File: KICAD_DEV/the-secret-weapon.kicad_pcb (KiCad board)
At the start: 6 copper layers, 150 x 150 mm, 43 parts, among them J1 USB_C_Receptacle_USB2.0_14P, J2 Screw_Terminal_01x02, SW1 SW_Push, SW2 SW_Push, U1 STM32H743VITx, U2 USBLC6-2SC6, U3 LMR33640ADDA, U4 LM1086S-3.3/TR, Y1 8 MHz, Y2 32.768 KHz

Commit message: heading to school!
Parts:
- moved F1 3.96 mm to (168.8, 165.2)
- moved J2 3.03 mm to (166.6, 172.9)
- moved C3 2.47 mm to (150.4, 170.1), turned to 90 degrees
- moved C1 2.20 mm to (156.6, 173.0), turned to 0 degrees
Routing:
- net Net-(U3-FB): track 0.00 -> 1.62 mm
- net GND: track 4.62 -> 3.56 mm, vias 8 -> 6

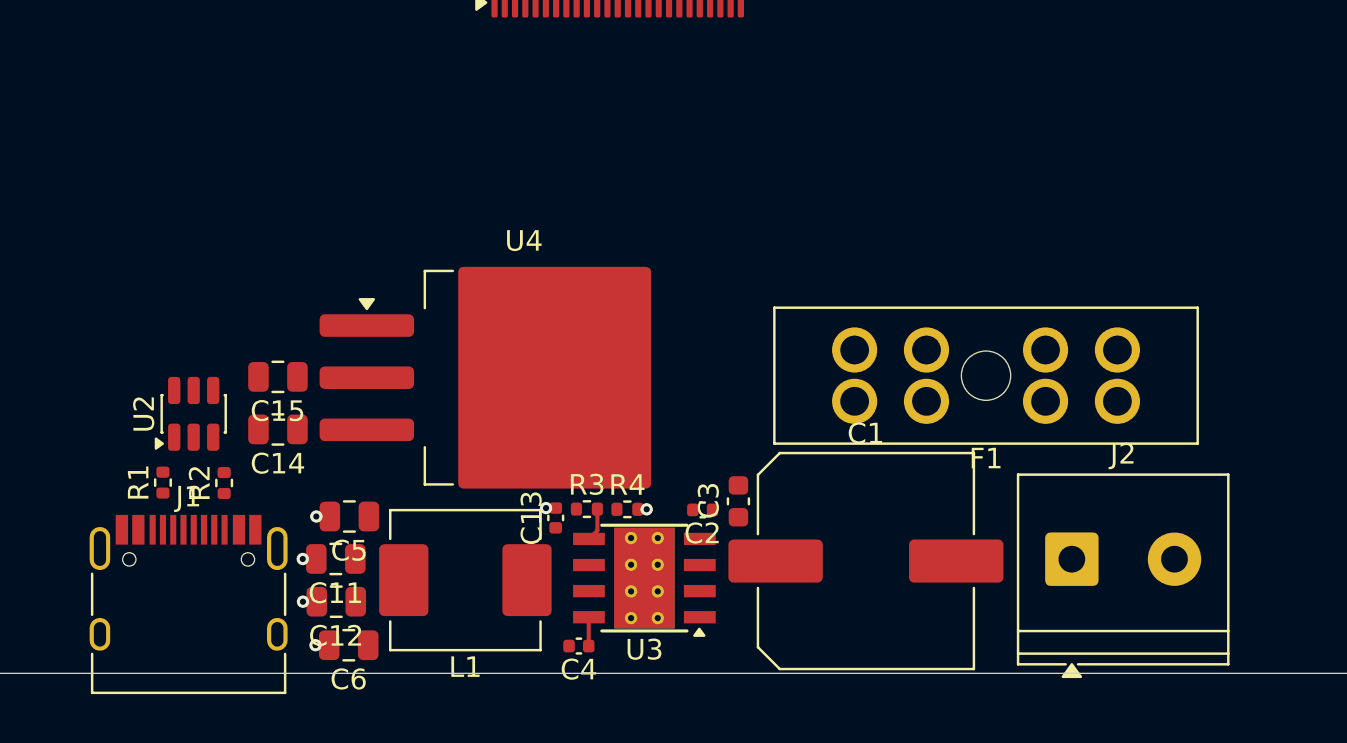
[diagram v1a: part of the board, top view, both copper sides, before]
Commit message: grounding and working on power, added the 100uF cap
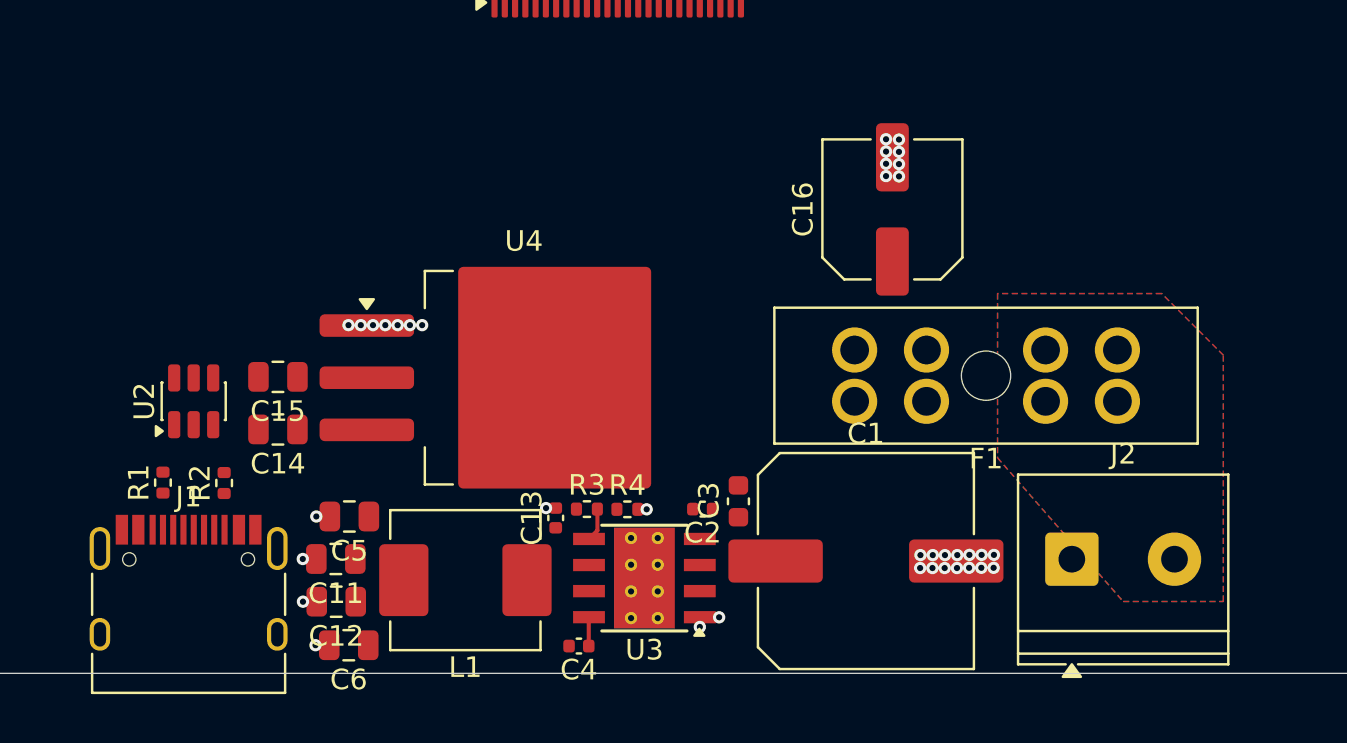
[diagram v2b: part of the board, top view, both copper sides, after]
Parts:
- added C16: 100uF, Capacitor_SMD:C_Elec_6.3x5.8, F.Cu at (157.9, 155.9)
- moved U2 0.61 mm to (123.8, 165.2)
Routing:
- net GND: track 3.56 -> 4.98 mm, vias 6 -> 37
- added copper zone on B.Cu, net Net-(J2-Pin_2)
- added copper zone on F.Cu, net Net-(J2-Pin_2)

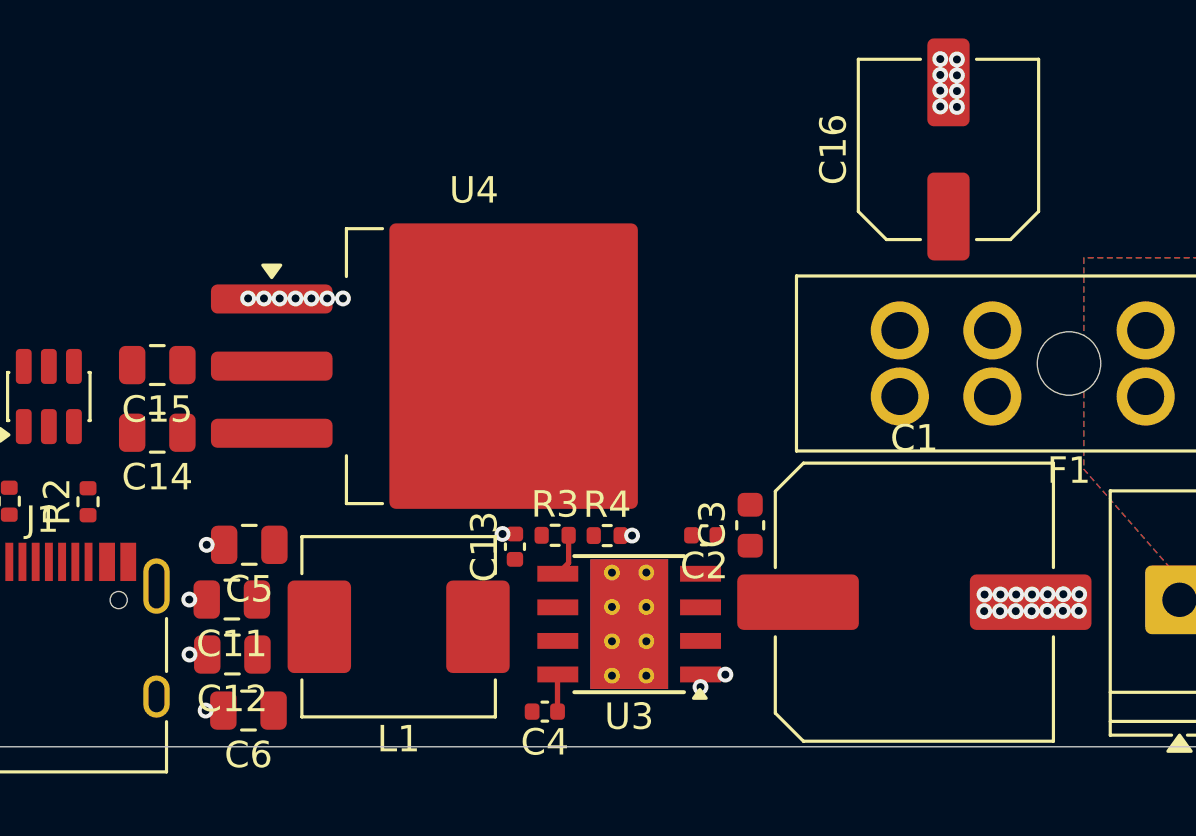
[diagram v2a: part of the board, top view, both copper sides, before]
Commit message: adding the power fills
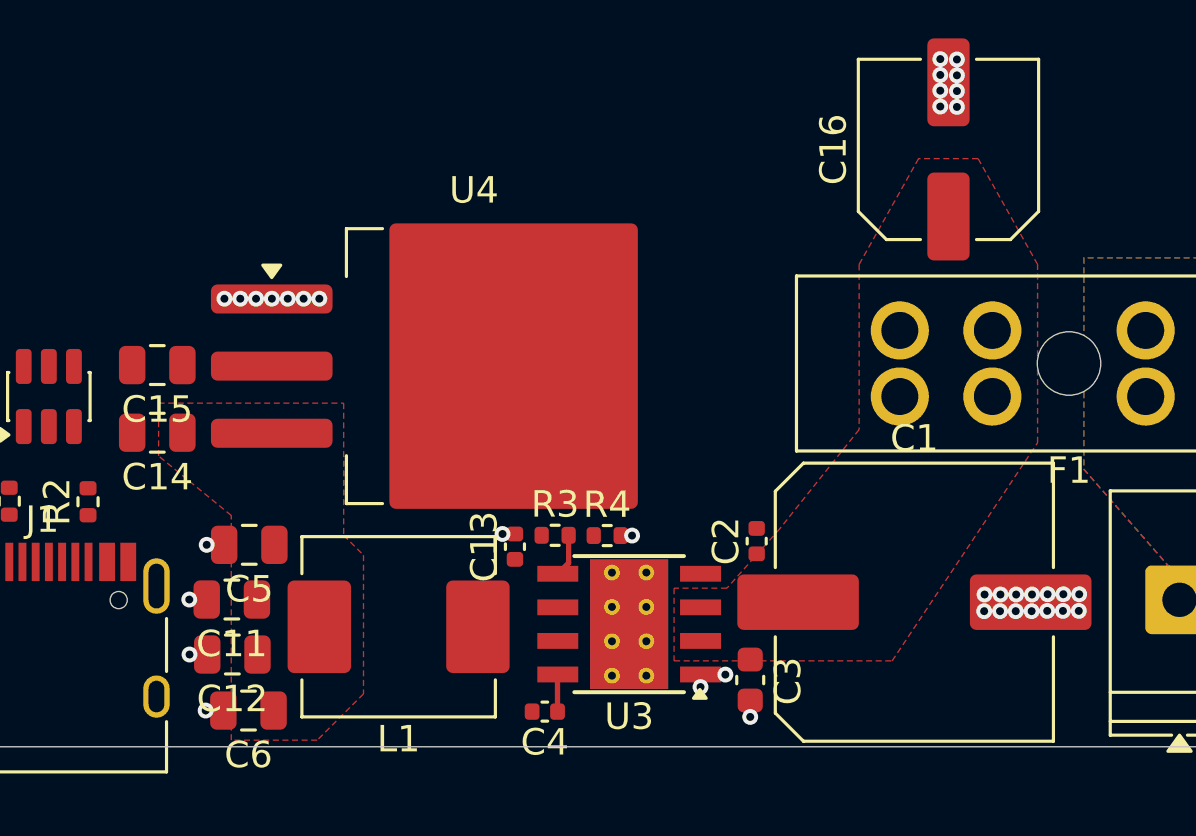
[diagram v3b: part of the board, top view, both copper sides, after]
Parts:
- moved C3 5.85 mm to (150.4, 176.0), turned to -90 degrees
- moved C2 2.00 mm to (150.6, 170.7), turned to 90 degrees
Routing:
- net GND: track 4.98 -> 5.60 mm, vias 37 -> 38
- added copper zone on F.Cu, net +12V
- added copper zone on F.Cu, net +5V
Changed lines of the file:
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@@
 	(footprint "Capacitor_SMD:C_0402_1005Metric"
 		(layer "F.Cu")
-		(at 148.64 170.5 180)
+		(at 150.625 170.72 90)
 		(descr "Capacitor SMD 0402 (1005 Metric), square (rectangular) end terminal, IPC-7351 nominal, (Body size source: IPC-SM-782 page 76, https://www.pcb-3d.com/wordpress/wp-content/uploads/ipc-sm-782a_amendment_1_and_2.pdf), generated with kicad-footprint-generator")
 		(tags "capacitor")
 		(property "Reference" "C2"
-			(at 0 -1.16 0)
+			(at 0 -1.16 90)
 			(layer "F.SilkS")
 			(effects
@@
 		)
 		(property "Value" "220nF"
-			(at 0 1.16 0)
+			(at 0 1.16 90)
 			(layer "F.Fab")
 			(effects
@@
 		)
 		(property "Datasheet" "~"
-			(at 0 0 0)
+			(at 0 0 90)
 			(layer "F.Fab")
 			(hide yes)
@@
 		)
 		(property "Description" "Unpolarized capacitor"
-			(at 0 0 0)
+			(at 0 0 90)
 			(layer "F.Fab")
 			(hide yes)
@@
 		(attr smd)
 		(fp_line
-			(start -0.107836 0.36)
-			(end 0.107836 0.36)
+			(start -0.107836 -0.36)
+			(end 0.107836 -0.36)
 			(stroke
 				(width 0.12)
@@
 		)
 		(fp_line
-			(start -0.107836 -0.36)
-			(end 0.107836 -0.36)
+			(start -0.107836 0.36)
+			(end 0.107836 0.36)
 			(stroke
 				(width 0.12)
@@
 		)
 		(fp_line
-			(start 0.91 0.46)
-			(end -0.91 0.46)
+			(start 0.91 -0.46)
+			(end 0.91 0.46)
 			(stroke
 				(width 0.05)
@@
 		)
 		(fp_line
-			(start 0.91 -0.46)
-			(end 0.91 0.46)
+			(start -0.91 -0.46)
+			(end 0.91 -0.46)
 			(stroke
 				(width 0.05)
@@
 		)
 		(fp_line
-			(start -0.91 0.46)
-			(end -0.91 -0.46)
+			(start 0.91 0.46)
+			(end -0.91 0.46)
 			(stroke
 				(width 0.05)
@@
 		)
 		(fp_line
-			(start -0.91 -0.46)
-			(end 0.91 -0.46)
+			(start -0.91 0.46)
+			(end -0.91 -0.46)
 			(stroke
 				(width 0.05)
@@
 		)
 		(fp_line
-			(start 0.5 0.25)
-			(end -0.5 0.25)
+			(start 0.5 -0.25)
+			(end 0.5 0.25)
 			(stroke
 				(width 0.1)
@@
 		)
 		(fp_line
-			(start 0.5 -0.25)
-			(end 0.5 0.25)
+			(start -0.5 -0.25)
+			(end 0.5 -0.25)
 			(stroke
 				(width 0.1)
@@
 		)
 		(fp_line
-			(start -0.5 0.25)
-			(end -0.5 -0.25)
+			(start 0.5 0.25)
+			(end -0.5 0.25)
 			(stroke
 				(width 0.1)
@@
 		)
 		(fp_line
-			(start -0.5 -0.25)
-			(end 0.5 -0.25)
+			(start -0.5 0.25)
+			(end -0.5 -0.25)
 			(stroke
 				(width 0.1)
@@
 		)
 		(fp_text user "${REFERENCE}"
-			(at 0 0 0)
+			(at 0 0 90)
 			(layer "F.Fab")
 			(effects
@@
 		)
 		(pad "1" smd roundrect
-			(at -0.48 0 180)
+			(at -0.48 0 90)
 			(size 0.56 0.62)
 			(layers "F.Cu" "F.Mask" "F.Paste")
@@
 		)
 		(pad "2" smd roundrect
-			(at 0.48 0 180)
+			(at 0.48 0 90)
 			(size 0.56 0.62)
 			(layers "F.Cu" "F.Mask" "F.Paste")
@@
 	(footprint "Capacitor_SMD:C_0603_1608Metric"
 		(layer "F.Cu")
-		(at 150.38 170.12 90)
+		(at 150.38 175.975 -90)
 		(descr "Capacitor SMD 0603 (1608 Metric), square (rectangular) end terminal, IPC-7351 nominal, (Body size source: IPC-SM-782 page 76, https://www.pcb-3d.com/wordpress/wp-content/uploads/ipc-sm-782a_amendment_1_and_2.pdf), generated with kicad-footprint-generator")
 		(tags "capacitor")
@@
 		(attr smd)
 		(fp_line
-			(start -0.14058 -0.51)
-			(end 0.14058 -0.51)
+			(start -0.14058 0.51)
+			(end 0.14058 0.51)
 			(stroke
 				(width 0.12)
@@
 		)
 		(fp_line
-			(start -0.14058 0.51)
-			(end 0.14058 0.51)
+			(start -0.14058 -0.51)
+			(end 0.14058 -0.51)
 			(stroke
 				(width 0.12)
@@
 		)
 		(fp_line
-			(start 1.48 -0.73)
-			(end 1.48 0.73)
+			(start -1.48 0.73)
+			(end -1.48 -0.73)
 			(stroke
 				(width 0.05)
@@
 		)
 		(fp_line
-			(start -1.48 -0.73)
-			(end 1.48 -0.73)
+			(start 1.48 0.73)
+			(end -1.48 0.73)
 			(stroke
 				(width 0.05)
@@
 		)
 		(fp_line
-			(start 1.48 0.73)
-			(end -1.48 0.73)
+			(start -1.48 -0.73)
+			(end 1.48 -0.73)
 			(stroke
 				(width 0.05)
@@
 		)
 		(fp_line
-			(start -1.48 0.73)
-			(end -1.48 -0.73)
+			(start 1.48 -0.73)
+			(end 1.48 0.73)
 			(stroke
 				(width 0.05)
@@
 		)
 		(fp_line
-			(start 0.8 -0.4)
-			(end 0.8 0.4)
+			(start -0.8 0.4)
+			(end -0.8 -0.4)
 			(stroke
 				(width 0.1)
@@
 		)
 		(fp_line
-			(start -0.8 -0.4)
-			(end 0.8 -0.4)
+			(start 0.8 0.4)
+			(end -0.8 0.4)
 			(stroke
 				(width 0.1)
@@
 		)
 		(fp_line
-			(start 0.8 0.4)
-			(end -0.8 0.4)
+			(start -0.8 -0.4)
+			(end 0.8 -0.4)
 			(stroke
 				(width 0.1)
@@
 		)
 		(fp_line
-			(start -0.8 0.4)
-			(end -0.8 -0.4)
+			(start 0.8 -0.4)
+			(end 0.8 0.4)
 			(stroke
 				(width 0.1)
@@
 		)
 		(pad "1" smd roundrect
-			(at -0.775 0 90)
+			(at -0.775 0 270)
 			(size 0.9 0.95)
 			(layers "F.Cu" "F.Mask" "F.Paste")
@@
 		)
 		(pad "2" smd roundrect
-			(at 0.775 0 90)
+			(at 0.775 0 270)
 			(size 0.9 0.95)
 			(layers "F.Cu" "F.Mask" "F.Paste")
@@
 	)
 	(segment
+		(start 150.38 176.75)
+		(end 150.38 177.37)
+		(width 0.2)
+		(layer "F.Cu")
+		(net 1)
+	)
+	(segment
 		(start 129.84 175.01)
 		(end 129.17 175.01)
@@
 	)
 	(via
-		(at 132.58 161.54)
+		(at 131.685 161.55)
 		(size 0.6)
 		(drill 0.3)
@@
 	)
 	(via
-		(at 133.78 161.54)
+		(at 132.885 161.55)
+		(size 0.6)
+		(drill 0.3)
+		(layers "F.Cu" "B.Cu")
+		(net 1)
+	)
+	(via
+		(at 150.38 177.37)
 		(size 0.6)
 		(drill 0.3)
@@
 	)
 	(via
-		(at 133.18 161.54)
+		(at 132.285 161.55)
 		(size 0.6)
 		(drill 0.3)
@@
 	)
 	(via
-		(at 131.385 161.54)
+		(at 130.49 161.55)
 		(size 0.6)
 		(drill 0.3)
@@
 	)
 	(via
-		(at 131.985 161.54)
+		(at 131.09 161.55)
 		(size 0.6)
 		(drill 0.3)
@@
 	)
 	(via
-		(at 134.975 161.54)
+		(at 134.08 161.55)
 		(size 0.6)
 		(drill 0.3)
@@
 	)
 	(via
-		(at 134.38 161.54)
+		(at 133.485 161.55)
 		(size 0.6)
 		(drill 0.3)
@@
 	)
 	(zone
+		(net 90)
+		(net_name "+5V")
+		(layer "F.Cu")
+		(hatch edge 0.5)
+		(priority 3)
+		(connect_pads
+			(clearance 0.2)
+		)
+		(min_thickness 0.25)
+		(filled_areas_thickness no)
+		(fill yes
+			(thermal_gap 0.15)
+			(thermal_bridge_width 1)
+		)
+		(polygon
+			(pts
+				(xy 135 165.5) (xy 135 170.5) (xy 135.75 171.25) (xy 135.75 176.5) (xy 134 178.25) (xy 130.75 178.25)
+				(xy 130.75 169.75) (xy 128 167.5) (xy 128 165.5)
+			)
+		)
+	)
+	(zone
+		(net 94)
+		(net_name "+12V")
+		(layer "F.Cu")
+		(hatch edge 0.5)
+		(priority 2)
+		(connect_pads
+			(clearance 0.2)
+		)
+		(min_thickness 0.25)
+		(filled_areas_thickness no)
+		(fill yes
+			(thermal_gap 0.15)
+			(thermal_bridge_width 1)
+		)
+		(polygon
+			(pts
+				(xy 147.5 172.5) (xy 147.5 175.25) (xy 155.75 175.25) (xy 161.25 167) (xy 161.25 160.25) (xy 159 156.25)
+				(xy 156.75 156.25) (xy 154.5 160.25) (xy 154.5 166.5) (xy 151.5 170.25) (xy 149.5 172.5) (xy 149.5 172.5)
+				(xy 149.5 172.5) (xy 149.5 172.5)
+			)
+		)
+	)
+	(zone
 		(net 97)
 		(net_name "Net-(J2-Pin_2)")
@@
 		(fill yes
 			(thermal_gap 0.5)
-			(thermal_bridge_width 0.5)
+			(thermal_bridge_width 1)
 		)
 		(polygon

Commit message: working on some more routing!
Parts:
- moved C13 6.95 mm to (144.6, 177.2), turned to 0 degrees
- moved C12 0.42 mm to (131.2, 175.0)
- moved J1 0.42 mm to (124.0, 175.5)
- moved R1 0.42 mm to (122.8, 169.2)
- moved C14 0.42 mm to (128.4, 166.6)
- moved C15 0.42 mm to (128.4, 164.1)
- moved R2 0.42 mm to (125.8, 169.2)
- moved U2 0.42 mm to (124.3, 165.2)
- moved C11 0.42 mm to (131.2, 172.9)
- moved C5 0.42 mm to (131.8, 170.8)
- moved L1 0.42 mm to (137.5, 173.9)
- moved C6 0.42 mm to (131.8, 177.1)
- moved U4 0.42 mm to (140.3, 164.1)
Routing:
- net +5V: track 0.00 -> 18.4 mm
- net USB_D-: track 0.00 -> 8.57 mm
- net USB_D+: track 0.00 -> 8.57 mm
- net GND: track 5.60 -> 11.6 mm, vias 38 -> 43
- net Net-(U3-VCC): track 0.00 -> 5.32 mm, vias 0 -> 2
- net Net-(J1-CC1): track 0.00 -> 1.78 mm
- net Net-(J1-CC2): track 0.00 -> 1.77 mm
- added copper zone on B.Cu, net +12V
- added copper zone on F.Cu, net Net-(U3-BOOT)
